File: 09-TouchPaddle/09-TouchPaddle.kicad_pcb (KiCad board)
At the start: 2 copper layers, 40 x 22 mm, 3 parts

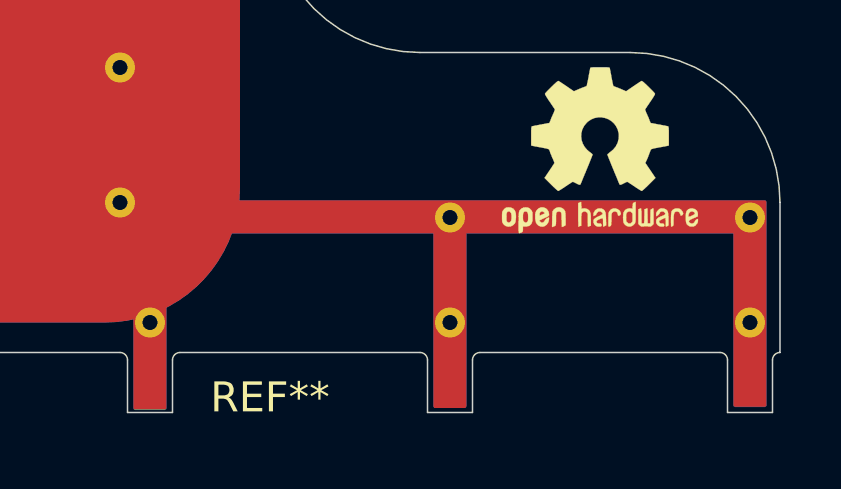
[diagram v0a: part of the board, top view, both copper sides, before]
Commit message: Update key and paddle to add more solder pads to improve mounting
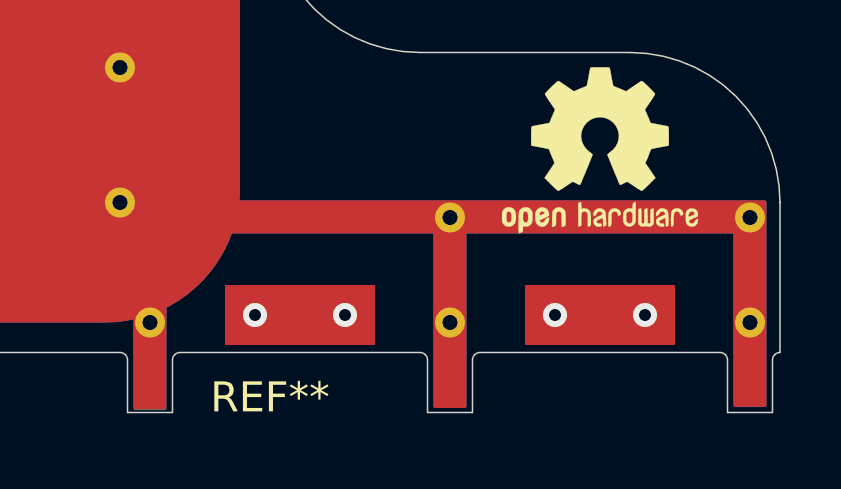
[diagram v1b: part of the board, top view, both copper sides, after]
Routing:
- net (no net): vias 0 -> 4
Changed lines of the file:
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@@
       (drillshape 0)
       (scaleselection 1)
-      (outputdirectory "")
+      (outputdirectory "gerber")
     )
   )
@@
       (xy -8.501079 -7.017353)
       (xy 15.998921 -7.017353)) (layer "B.Cu") (width 0.1) (fill solid))
-    (fp_rect (start -5.04 -2.96) (end -3.96 -0.09) (layer "B.Mask") (width 0.1) (fill solid))
     (fp_rect (start 15 -2.96) (end 16.03 -0.21) (layer "B.Mask") (width 0.1) (fill solid))
     (fp_rect (start 4.95 -2.96) (end 6.04 -0.17) (layer "B.Mask") (width 0.1) (fill solid))
+    (fp_rect (start -5.04 -2.96) (end -3.96 -0.09) (layer "B.Mask") (width 0.1) (fill solid))
     (fp_rect (start 15 -2.96) (end 16.03 -0.22) (layer "F.Mask") (width 0.1) (fill solid))
+    (fp_rect (start 5 -2.97) (end 6.04 -0.16) (layer "F.Mask") (width 0.1) (fill solid))
     (fp_rect (start -5.02 -2.97) (end -3.99 -0.1) (layer "F.Mask") (width 0.1) (fill solid))
-    (fp_rect (start 5 -2.97) (end 6.04 -0.16) (layer "F.Mask") (width 0.1) (fill solid))
-    (fp_line (start 16.5 -7) (end 16.5 0) (layer "Dwgs.User") (width 0.12))
-    (fp_line (start 14.5 0) (end 16.5 0) (layer "Dwgs.User") (width 0.12))
-    (fp_line (start 4.5 -2) (end -3.5 -2) (layer "Dwgs.User") (width 0.12))
+    (fp_line (start 14.5 -2) (end 6.5 -2) (layer "Dwgs.User") (width 0.12))
+    (fp_line (start -5.5 -2) (end -18.5 -2) (layer "Dwgs.User") (width 0.12))
+    (fp_line (start 14.5 0) (end 14.5 -2) (layer "Dwgs.User") (width 0.12))
+    (fp_line (start 4.5 -12) (end 11.5 -12) (layer "Dwgs.User") (width 0.12))
     (fp_line (start 4.5 0) (end 4.5 -2) (layer "Dwgs.User") (width 0.12))
-    (fp_line (start 14.5 0) (end 14.5 -2) (layer "Dwgs.User") (width 0.12))
     (fp_line (start -3.5 -2) (end -3.5 0) (layer "Dwgs.User") (width 0.12))
-    (fp_line (start -5.5 0) (end -3.5 0) (layer "Dwgs.User") (width 0.12))
+    (fp_line (start -5.5 -0.017804) (end -5.5 -2) (layer "Dwgs.User") (width 0.12))
     (fp_line (start 6.5 -2) (end 6.5 0) (layer "Dwgs.User") (width 0.12))
     (fp_line (start 4.5 0) (end 6.5 0) (layer "Dwgs.User") (width 0.12))
     (fp_line (start -23.5 -7) (end -23.5 -17) (layer "Dwgs.User") (width 0.12))
-    (fp_line (start -5.5 -0.017804) (end -5.5 -2) (layer "Dwgs.User") (width 0.12))
-    (fp_line (start 4.5 -12) (end 11.5 -12) (layer "Dwgs.User") (width 0.12))
-    (fp_line (start -5.5 -2) (end -18.5 -2) (layer "Dwgs.User") (width 0.12))
-    (fp_line (start 14.5 -2) (end 6.5 -2) (layer "Dwgs.User") (width 0.12))
+    (fp_line (start 4.5 -2) (end -3.5 -2) (layer "Dwgs.User") (width 0.12))
+    (fp_line (start 16.5 -7) (end 16.5 0) (layer "Dwgs.User") (width 0.12))
     (fp_line (start -18.5 -22) (end -5.5 -22) (layer "Dwgs.User") (width 0.12))
+    (fp_line (start -5.5 0) (end -3.5 0) (layer "Dwgs.User") (width 0.12))
+    (fp_line (start 14.5 0) (end 16.5 0) (layer "Dwgs.User") (width 0.12))
+    (fp_arc (start -5.5 -17) (end -5.5 -22) (angle 90) (layer "Dwgs.User") (width 0.12))
     (fp_arc (start -18.5 -17) (end -23.5 -17) (angle 90) (layer "Dwgs.User") (width 0.12))
-    (fp_arc (start -5.5 -17) (end -5.5 -22) (angle 90) (layer "Dwgs.User") (width 0.12))
     (fp_arc (start 4.5 -17) (end 4.5 -12) (angle 90) (layer "Dwgs.User") (width 0.12))
+    (fp_arc (start 11.5 -7) (end 11.5 -12) (angle 90) (layer "Dwgs.User") (width 0.12))
     (fp_arc (start -18.5 -7) (end -18.5 -2) (angle 90) (layer "Dwgs.User") (width 0.12))
-    (fp_arc (start 11.5 -7) (end 11.5 -12) (angle 90) (layer "Dwgs.User") (width 0.12))
-    (fp_line (start 16.25 0) (end 14.75 0) (layer "Edge.Cuts") (width 0.05))
-    (fp_line (start 6.5 -2) (end 14.5 -2) (layer "Edge.Cuts") (width 0.05))
-    (fp_line (start -23.5 -17) (end -23.5 -7) (layer "Edge.Cuts") (width 0.05))
-    (fp_line (start 6.25 -1.75) (end 6.25 0) (layer "Edge.Cuts") (width 0.05))
     (fp_line (start 4.5 -12) (end 11.5 -12) (layer "Edge.Cuts") (width 0.05))
-    (fp_line (start 16.25 -1.75) (end 16.25 0) (layer "Edge.Cuts") (width 0.05))
-    (fp_line (start -5.5 -2) (end -18.5 -2) (layer "Edge.Cuts") (width 0.05))
-    (fp_line (start 4.5 -2) (end -3.5 -2) (layer "Edge.Cuts") (width 0.05))
-    (fp_line (start -18.5 -22) (end -5.5 -22) (layer "Edge.Cuts") (width 0.05))
-    (fp_line (start 14.75 0) (end 14.75 -1.75) (layer "Edge.Cuts") (width 0.05))
-    (fp_line (start 16.5 -7) (end 16.5 -2) (layer "Edge.Cuts") (width 0.05))
-    (fp_line (start 6.25 0) (end 4.75 0) (layer "Edge.Cuts") (width 0.05))
-    (fp_line (start -3.75 0) (end -5.25 0) (layer "Edge.Cuts") (width 0.05))
     (fp_line (start 4.75 0) (end 4.75 -1.75) (layer "Edge.Cuts") (width 0.05))
     (fp_line (start -3.75 -1.75) (end -3.75 0) (layer "Edge.Cuts") (width 0.05))
+    (fp_line (start -3.75 0) (end -5.25 0) (layer "Edge.Cuts") (width 0.05))
+    (fp_line (start -18.5 -22) (end -5.5 -22) (layer "Edge.Cuts") (width 0.05))
+    (fp_line (start 16.25 0) (end 14.75 0) (layer "Edge.Cuts") (width 0.05))
+    (fp_line (start -23.5 -17) (end -23.5 -7) (layer "Edge.Cuts") (width 0.05))
+    (fp_line (start -5.5 -2) (end -18.5 -2) (layer "Edge.Cuts") (width 0.05))
+    (fp_line (start 6.5 -2) (end 14.5 -2) (layer "Edge.Cuts") (width 0.05))
+    (fp_line (start 4.5 -2) (end -3.5 -2) (layer "Edge.Cuts") (width 0.05))
+    (fp_line (start 16.25 -1.75) (end 16.25 0) (layer "Edge.Cuts") (width 0.05))
     (fp_line (start -5.25 0) (end -5.25 -1.75) (layer "Edge.Cuts") (width 0.05))
-    (fp_arc (start 4.5 -17) (end -0.5 -17) (angle -90) (layer "Edge.Cuts") (width 0.05))
-    (fp_arc (start 16.5 -1.75) (end 16.5 -2) (angle -90) (layer "Edge.Cuts") (width 0.05))
+    (fp_line (start 6.25 -1.75) (end 6.25 0) (layer "Edge.Cuts") (width 0.05))
+    (fp_line (start 16.5 -7) (end 16.5 -2) (layer "Edge.Cuts") (width 0.05))
+    (fp_line (start 14.75 0) (end 14.75 -1.75) (layer "Edge.Cuts") (width 0.05))
+    (fp_line (start 6.25 0) (end 4.75 0) (layer "Edge.Cuts") (width 0.05))
     (fp_arc (start 4.5 -1.75) (end 4.75 -1.75) (angle -90) (layer "Edge.Cuts") (width 0.05))
-    (fp_arc (start 6.5 -1.75) (end 6.5 -2) (angle -90) (layer "Edge.Cuts") (width 0.05))
+    (fp_arc (start -3.5 -1.75) (end -3.5 -2) (angle -90) (layer "Edge.Cuts") (width 0.05))
     (fp_arc (start 14.5 -1.75) (end 14.75 -1.75) (angle -90) (layer "Edge.Cuts") (width 0.05))
-    (fp_arc (start -3.5 -1.75) (end -3.5 -2) (angle -90) (layer "Edge.Cuts") (width 0.05))
-    (fp_arc (start -18.5 -7) (end -23.5 -7) (angle -90) (layer "Edge.Cuts") (width 0.05))
-    (fp_arc (start -18.5 -17) (end -18.5 -22) (angle -90) (layer "Edge.Cuts") (width 0.05))
     (fp_arc (start 11.5 -7) (end 16.5 -7) (angle -90) (layer "Edge.Cuts") (width 0.05))
     (fp_arc (start -5.5 -17) (end -0.5 -17) (angle -90) (layer "Edge.Cuts") (width 0.05))
+    (fp_arc (start -18.5 -17) (end -18.5 -22) (angle -90) (layer "Edge.Cuts") (width 0.05))
     (fp_arc (start -5.5 -1.75) (end -5.25 -1.75) (angle -90) (layer "Edge.Cuts") (width 0.05))
+    (fp_arc (start 16.5 -1.75) (end 16.5 -2) (angle -90) (layer "Edge.Cuts") (width 0.05))
+    (fp_arc (start 4.5 -17) (end -0.5 -17) (angle -90) (layer "Edge.Cuts") (width 0.05))
+    (fp_arc (start 6.5 -1.75) (end 6.5 -2) (angle -90) (layer "Edge.Cuts") (width 0.05))
+    (fp_arc (start -18.5 -7) (end -23.5 -7) (angle -90) (layer "Edge.Cuts") (width 0.05))
+    (pad "1" thru_hole circle (at -5.5 -7) (size 1 1) (drill 0.5) (layers *.Cu *.Mask))
+    (pad "1" thru_hole circle (at -4.5 -3) (size 1 1) (drill 0.5) (layers *.Cu *.Mask))
+    (pad "1" smd roundrect (at -12 -12) (size 21 18) (layers "B.Cu" "B.Mask") (roundrect_rratio 0.25))
+    (pad "1" thru_hole circle (at -5.5 -11.5) (size 1 1) (drill 0.5) (layers *.Cu *.Mask))
     (pad "1" smd roundrect (at -12 -12) (size 21 18) (layers "F.Cu" "F.Mask") (roundrect_rratio 0.25))
-    (pad "1" thru_hole circle (at -5.5 -7) (size 1 1) (drill 0.5) (layers *.Cu *.Mask))
+    (pad "1" thru_hole circle (at -18.5 -7) (size 1 1) (drill 0.5) (layers *.Cu *.Mask))
+    (pad "1" thru_hole circle (at -12 -7) (size 1 1) (drill 0.5) (layers *.Cu *.Mask))
+    (pad "1" thru_hole circle (at -5.5 -16.5) (size 1 1) (drill 0.5) (layers *.Cu *.Mask))
+    (pad "1" thru_hole circle (at 5.5 -3) (size 1 1) (drill 0.5) (layers *.Cu *.Mask))
     (pad "1" thru_hole circle (at 5.5 -6.5) (size 1 1) (drill 0.5) (layers *.Cu *.Mask))
-    (pad "1" thru_hole circle (at -4.5 -3) (size 1 1) (drill 0.5) (layers *.Cu *.Mask))
-    (pad "1" thru_hole circle (at -5.5 -11.5) (size 1 1) (drill 0.5) (layers *.Cu *.Mask))
     (pad "1" thru_hole circle (at 15.5 -6.5) (size 1 1) (drill 0.5) (layers *.Cu *.Mask))
     (pad "1" thru_hole circle (at 15.5 -3) (size 1 1) (drill 0.5) (layers *.Cu *.Mask))
-    (pad "1" thru_hole circle (at -5.5 -16.5) (size 1 1) (drill 0.5) (layers *.Cu *.Mask))
-    (pad "1" thru_hole circle (at 5.5 -3) (size 1 1) (drill 0.5) (layers *.Cu *.Mask))
-    (pad "1" thru_hole circle (at -12 -7) (size 1 1) (drill 0.5) (layers *.Cu *.Mask))
-    (pad "1" thru_hole circle (at -18.5 -7) (size 1 1) (drill 0.5) (layers *.Cu *.Mask))
-    (pad "1" smd roundrect (at -12 -12) (size 21 18) (layers "B.Cu" "B.Mask") (roundrect_rratio 0.25))
+    (pad "2" smd rect (at 10.5 -3.25) (size 5 2) (layers "F.Cu" "F.Mask"))
+    (pad "2" smd rect (at 10.5 -3.25) (size 5 2) (layers "B.Cu" "B.Mask"))
+    (pad "2" smd rect (at 0.5 -3.25) (size 5 2) (layers "B.Cu" "B.Mask"))
+    (pad "2" smd rect (at 0.5 -3.25) (size 5 2) (layers "F.Cu" "F.Mask"))
   )
   (footprint "Symbol:OSHW-Logo2_7.3x6mm_SilkScreen" (layer "F.Cu")
@@
       (xy 3.153595 -1.966966)) (layer "B.SilkS") (width 0.01) (fill solid))
   )
+  (via (at 162 91.5) (size 0.8) (drill 0.4) (layers "F.Cu" "B.Cu") (net 0))
+  (via (at 159 91.5) (size 0.8) (drill 0.4) (layers "F.Cu" "B.Cu") (net 0))
+  (via (at 152 91.5) (size 0.8) (drill 0.4) (layers "F.Cu" "B.Cu") (net 0))
+  (via (at 149 91.5) (size 0.8) (drill 0.4) (layers "F.Cu" "B.Cu") (net 0))
 )
